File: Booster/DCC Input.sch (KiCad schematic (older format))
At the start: 18 parts, among them P201 CONN_01X02, P202 CONN_01X02, SW601 DIP, U201 6N137, U203 LM339, U701 74HC86

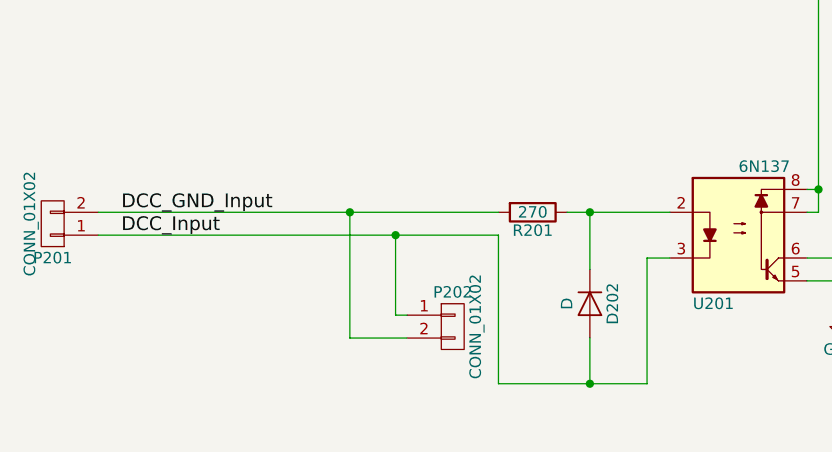
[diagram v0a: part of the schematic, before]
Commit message: Fixed DCC input direction through optocoupler reversed.
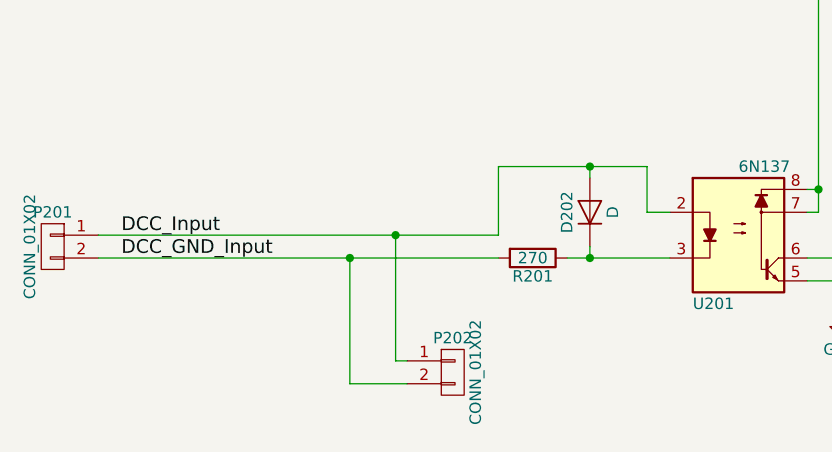
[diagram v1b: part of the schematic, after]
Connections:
- net DCC_Input: now also U201.2; no longer U201.3
- net at D202.1 (K), R201.1: now also U201.3; no longer U201.2
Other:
- moved on the sheet: D202, P201, P202, R201
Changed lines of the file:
@@
 L R R201
 U 1 1 59E8F235
-P 3450 4800
-F 0 "R201" V 3530 4800 50  0000 C CNN
-F 1 "270" V 3450 4800 50  0000 C CNN
-F 2 "Resistors_SMD:R_0805" V 3380 4800 50  0001 C CNN
-F 3 "" H 3450 4800 50  0001 C CNN
-	1    3450 4800
+P 3450 5000
+F 0 "R201" V 3530 5000 50  0000 C CNN
+F 1 "270" V 3450 5000 50  0000 C CNN
+F 2 "Resistors_SMD:R_0805" V 3380 5000 50  0001 C CNN
+F 3 "" H 3450 5000 50  0001 C CNN
+	1    3450 5000
 	0    1    1    0
 $EndComp
@@
 	1    0    0    -1
 $EndComp
-Text Label 1650 4800 0    60   ~ 0
+Text Label 1650 5000 0    60   ~ 0
 DCC_GND_Input
 Text Label 1650 4900 0    60   ~ 0
@@
 L CONN_01X02 P202
 U 1 1 5A39234E
-P 3100 5300
-F 0 "P202" H 3100 5450 50  0000 C CNN
-F 1 "CONN_01X02" V 3200 5300 50  0000 C CNN
-F 2 "Connectors_JST:JST_XH_B02B-XH-A_02x2.50mm_Straight" H 3100 5300 50  0001 C CNN
-F 3 "" H 3100 5300 50  0000 C CNN
-	1    3100 5300
+P 3100 5500
+F 0 "P202" H 3100 5650 50  0000 C CNN
+F 1 "CONN_01X02" V 3200 5500 50  0000 C CNN
+F 2 "Connectors_JST:JST_XH_B02B-XH-A_02x2.50mm_Straight" H 3100 5500 50  0001 C CNN
+F 3 "" H 3100 5500 50  0000 C CNN
+	1    3100 5500
 	1    0    0    -1
 $EndComp
@@
 L CONN_01X02 P201
 U 1 1 5A39248A
-P 1350 4850
-F 0 "P201" H 1350 5000 50  0000 C CNN
-F 1 "CONN_01X02" V 1450 4850 50  0000 C CNN
-F 2 "Connectors_JST:JST_XH_B02B-XH-A_02x2.50mm_Straight" H 1350 4850 50  0001 C CNN
-F 3 "" H 1350 4850 50  0000 C CNN
-	1    1350 4850
-	-1   0    0    1
+P 1350 4950
+F 0 "P201" H 1350 5100 50  0000 C CNN
+F 1 "CONN_01X02" V 1450 4950 50  0000 C CNN
+F 2 "Connectors_JST:JST_XH_B02B-XH-A_02x2.50mm_Straight" H 1350 4950 50  0001 C CNN
+F 3 "" H 1350 4950 50  0000 C CNN
+	1    1350 4950
+	-1   0    0    -1
 $EndComp
 $Comp
@@
 	6800 5000 6800 4150
 Wire Wire Line
-	3600 4800 4050 4800
-Wire Wire Line
 	5400 4350 5400 4200
 Wire Wire Line
@@
 	7550 2450 7550 2550
 Wire Wire Line
-	3300 4900 3300 5550
+	3300 4900 3300 4600
 Connection ~ 6800 5000
 Connection ~ 7150 1850
@@
 Wire Wire Line
 	6900 1600 6900 2350
-Connection ~ 2650 4800
-Wire Wire Line
-	2650 5350 2900 5350
-Wire Wire Line
-	2650 4800 2650 5350
+Connection ~ 2650 5000
+Wire Wire Line
+	2650 5550 2900 5550
+Wire Wire Line
+	2650 5000 2650 5550
 Connection ~ 2850 4900
 Wire Wire Line
-	2850 5250 2850 4900
-Wire Wire Line
-	2900 5250 2850 5250
+	2850 5450 2850 4900
+Wire Wire Line
+	2900 5450 2850 5450
 Wire Wire Line
 	1550 4900 3300 4900
 Wire Wire Line
-	1550 4800 3300 4800
+	1550 5000 3300 5000
+Wire Wire Line
+	3300 4600 3950 4600
+Connection ~ 3700 5000
+Connection ~ 3700 4600
+Wire Wire Line
+	3600 5000 4050 5000
 $Comp
 L D D202
 U 1 1 5A411C39
-P 3700 5200
-F 0 "D202" H 3700 5300 50  0000 C CNN
-F 1 "D" H 3700 5100 50  0000 C CNN
-F 2 "Diodes_SMD:D_MiniMELF" H 3700 5200 50  0001 C CNN
-F 3 "" H 3700 5200 50  0000 C CNN
-	1    3700 5200
-	0    1    1    0
-$EndComp
-Wire Wire Line
-	3300 5550 3950 5550
-Wire Wire Line
-	3700 5550 3700 5350
-Wire Wire Line
-	3700 5050 3700 4800
-Connection ~ 3700 4800
-Wire Wire Line
-	3950 5550 3950 5000
-Wire Wire Line
-	3950 5000 4050 5000
-Connection ~ 3700 5550
+P 3700 4800
+F 0 "D202" H 3700 4900 50  0000 C CNN
+F 1 "D" H 3700 4700 50  0000 C CNN
+F 2 "Diodes_SMD:D_MiniMELF" H 3700 4800 50  0001 C CNN
+F 3 "" H 3700 4800 50  0000 C CNN
+	1    3700 4800
+	0    -1   -1   0
+$EndComp
+Wire Wire Line
+	3700 4650 3700 4600
+Wire Wire Line
+	3700 4950 3700 5000
+Wire Wire Line
+	3950 4600 3950 4800
+Wire Wire Line
+	3950 4800 4050 4800
 $EndSCHEMATC
